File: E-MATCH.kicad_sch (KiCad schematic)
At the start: 23 parts, among them IC1 NCV81071BZR2G, IC2 NCV81071BZR2G, J1 691210910002, J2 691210910002, J3 691210910002, J4 691210910002, J5 DC Jack, Q1 AOSP36326C, Q2 AOSP36326C, Q3 AOSP36326C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

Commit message: Schematic pdf now in the repository
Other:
- title: (none) -> E-match Firing Circuit
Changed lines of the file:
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@@
 	(generator_version "9.0")
 	(paper "A4")
+	(title_block
+		(title "E-match Firing Circuit")
+		(date "2026-01-29")
+		(rev "v1.0")
+	)
 	(rectangle
 		(start 203.708 12.9484)

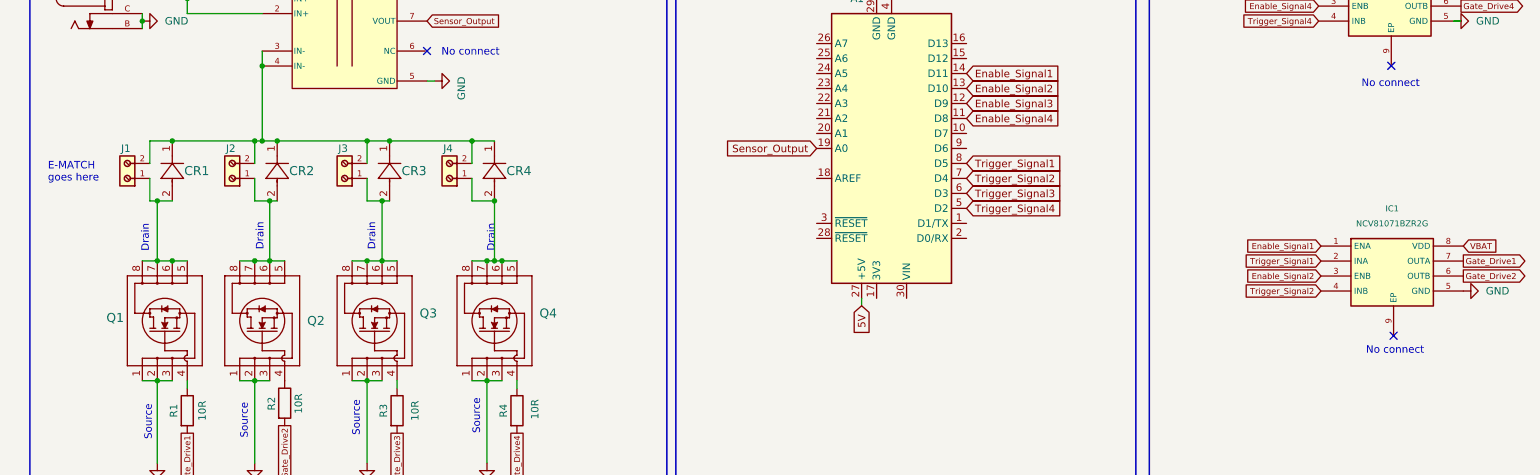
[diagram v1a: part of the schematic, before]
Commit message: modified some footprints
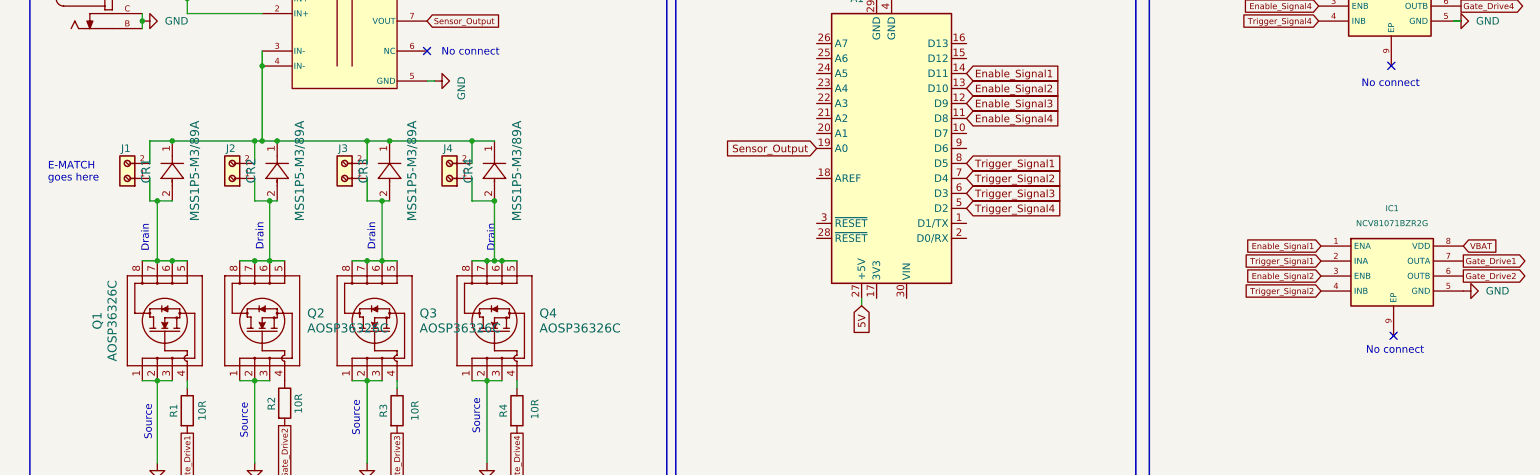
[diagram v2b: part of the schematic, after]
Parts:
- CR1, CR2, CR3, CR4: footprint (none) -> DIODE_MSP3V3
- IC1: footprint (none) -> SOP65P490X110-9N
- Q1, Q2, Q3, Q4: footprint (none) -> SO8SOP-8L_AOS
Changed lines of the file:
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@@
 		(dnp no)
 		(property "Reference" "CR2"
-			(at 57.912 78.74 90)
+			(at 51.435 78.74 0)
 			(effects
 				(font
 					(size 1.524 1.524)
 				)
-				(justify right)
 			)
 		)
 		(property "Value" "MSS1P5-M3/89A"
-			(at 59.69 80.0099 90)
+			(at 59.69 78.74 0)
 			(effects
 				(font
 					(size 1.524 1.524)
 				)
-				(justify right)
-				(hide yes)
-			)
-		)
-		(property "Footprint" ""
+			)
+		)
+		(property "Footprint" "DIODE_MSP3V3"
 			(at 55.88 83.82 0)
 			(effects
@@
 		(dnp no)
 		(property "Reference" "CR3"
-			(at 76.962 78.74 90)
+			(at 70.485 78.74 0)
 			(effects
 				(font
 					(size 1.524 1.524)
 				)
-				(justify right)
 			)
 		)
 		(property "Value" "MSS1P5-M3/89A"
-			(at 78.74 80.0099 90)
+			(at 78.74 78.74 0)
 			(effects
 				(font
 					(size 1.524 1.524)
 				)
-				(justify right)
-				(hide yes)
-			)
-		)
-		(property "Footprint" ""
+			)
+		)
+		(property "Footprint" "DIODE_MSP3V3"
 			(at 74.93 83.82 0)
 			(effects
@@
 		(dnp no)
 		(property "Reference" "CR1"
-			(at 40.132 78.74 90)
+			(at 33.655 78.74 0)
 			(effects
 				(font
 					(size 1.524 1.524)
 				)
-				(justify right)
 			)
 		)
 		(property "Value" "MSS1P5-M3/89A"
-			(at 41.91 80.0099 90)
+			(at 41.91 78.74 0)
 			(effects
 				(font
 					(size 1.524 1.524)
 				)
-				(justify right)
-				(hide yes)
-			)
-		)
-		(property "Footprint" ""
+			)
+		)
+		(property "Footprint" "DIODE_MSP3V3"
 			(at 38.1 83.82 0)
 			(effects
@@
 	)
 	(symbol
-		(lib_name "NCV81071BZR2G_1")
 		(lib_id "Gate Driver:NCV81071BZR2G")
 		(at 232.7997 91.4751 0)
@@
 		(fields_autoplaced yes)
 		(property "Reference" "IC1"
-			(at 244.8647 85.1251 0)
+			(at 244.8647 85.09 0)
 			(effects
 				(font
@@
 		)
 		(property "Value" "NCV81071BZR2G"
-			(at 244.8647 87.6651 0)
+			(at 244.8647 87.63 0)
 			(effects
 				(font
@@
 			)
 		)
-		(property "Footprint" ""
+		(property "Footprint" "SOP65P490X110-9N"
 			(at 259.4697 186.3951 0)
 			(effects
@@
 		(dnp no)
 		(property "Reference" "CR4"
-			(at 94.742 78.74 90)
+			(at 88.265 78.74 0)
 			(effects
 				(font
 					(size 1.524 1.524)
 				)
-				(justify right)
 			)
 		)
 		(property "Value" "MSS1P5-M3/89A"
-			(at 96.52 80.0099 90)
+			(at 96.52 78.74 0)
 			(effects
 				(font
 					(size 1.524 1.524)
 				)
-				(justify right)
-				(hide yes)
-			)
-		)
-		(property "Footprint" ""
+			)
+		)
+		(property "Footprint" "DIODE_MSP3V3"
 			(at 92.71 83.82 0)
 			(effects
@@
 	)
 	(symbol
-		(lib_name "AOSP36326C_1")
 		(lib_id "N-Ch Mosfet:AOSP36326C")
 		(at 88.9 119.38 90)
@@
 				)
 				(justify right)
-				(hide yes)
-			)
-		)
-		(property "Footprint" ""
+			)
+		)
+		(property "Footprint" "SO8SOP-8L_AOS"
 			(at 77.978 104.648 0)
 			(effects
@@
 	)
 	(symbol
-		(lib_name "AOSP36326C_1")
 		(lib_id "N-Ch Mosfet:AOSP36326C")
 		(at 68.58 119.38 90)
@@
 				)
 				(justify right)
-				(hide yes)
-			)
-		)
-		(property "Footprint" ""
+			)
+		)
+		(property "Footprint" "SO8SOP-8L_AOS"
 			(at 57.658 104.648 0)
 			(effects
@@
 		(dnp no)
 		(property "Reference" "Q1"
-			(at 26.924 103.632 90)
+			(at 25.4 104.14 0)
 			(effects
 				(font
 					(size 1.524 1.524)
 				)
-				(justify right)
 			)
 		)
 		(property "Value" "AOSP36326C"
-			(at 43.942 108.712 90)
+			(at 27.94 104.14 0)
 			(effects
 				(font
 					(size 1.524 1.524)
 				)
-				(justify right)
-				(hide yes)
-			)
-		)
-		(property "Footprint" ""
-			(at 28.702 104.14 0)
+			)
+		)
+		(property "Footprint" "SO8SOP-8L_AOS"
+			(at 22.098 104.648 0)
 			(effects
 				(font
@@
 		)
 		(property "Datasheet" "AOSP36326C"
-			(at 28.702 104.14 0)
+			(at 19.558 104.648 0)
 			(effects
 				(font
@@
 	)
 	(symbol
-		(lib_name "AOSP36326C_1")
 		(lib_id "N-Ch Mosfet:AOSP36326C")
 		(at 49.53 119.38 90)
@@
 		(fields_autoplaced yes)
 		(property "Reference" "Q2"
-			(at 60.96 104.1399 90)
+			(at 60.96 102.8699 90)
 			(effects
 				(font
@@
 				)
 				(justify right)
-				(hide yes)
-			)
-		)
-		(property "Footprint" ""
+			)
+		)
+		(property "Footprint" "SO8SOP-8L_AOS"
 			(at 38.608 104.648 0)
 			(effects

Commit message: Cleaned a few footprints
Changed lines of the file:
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@@
-	(wire
-		(pts
-			(xy 81.28 48.26) (xy 81.28 45.72)
-		)
-		(stroke
-			(width 0)
-			(type default)
-		)
-	)
 	(wire
 		(pts

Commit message: added a decoupling capacitor
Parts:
- added C1: 0.1u, 0.1 uF Cap:CAP_C0603C104K5RAC3121_KEM-L, symbol Device:C
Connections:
- net 5V: now also C1.2
- net GND: now also C1.1
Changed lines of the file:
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@@
+	)
+	(junction
+		(at 81.28 48.26)
+		(diameter 0)
+		(color 0 0 0 0)
 	)
 	(junction
@@
 	(wire
 		(pts
+			(xy 85.09 48.26) (xy 81.28 48.26)
+		)
+		(stroke
+			(width 0)
+			(type default)
+		)
+	)
+	(wire
+		(pts
 			(xy 71.12 114.3) (xy 71.12 128.27)
 		)
@@
 		(pts
 			(xy 88.9 83.82) (xy 92.71 83.82)
+		)
+		(stroke
+			(width 0)
+			(type default)
+		)
+	)
+	(wire
+		(pts
+			(xy 81.28 46.99) (xy 81.28 48.26)
 		)
 		(stroke
@@
 	(global_label "5V"
 		(shape input)
-		(at 81.28 48.26 0)
+		(at 85.09 48.26 0)
 		(fields_autoplaced yes)
 		(effects
@@
 		)
 		(property "Intersheetrefs" "${INTERSHEET_REFS}"
-			(at 85.5064 48.26 0)
+			(at 89.3164 48.26 0)
 			(effects
 				(font
@@
 				(path "/ac49d8b8-9946-4b6b-9646-a2b20606c52a"
 					(reference "#PWR08")
+					(unit 1)
+				)
+			)
+		)
+	)
+	(symbol
+		(lib_id "power:GND")
+		(at 81.28 39.37 180)
+		(unit 1)
+		(exclude_from_sim no)
+		(in_bom yes)
+		(on_board yes)
+		(dnp no)
+		(property "Reference" "#PWR011"
+			(at 81.28 33.02 0)
+			(effects
+				(font
+					(size 1.27 1.27)
+				)
+				(hide yes)
+			)
+		)
+		(property "Value" "GND"
+			(at 80.518 34.798 0)
+			(effects
+				(font
+					(size 1.27 1.27)
+				)
+				(justify right)
+			)
+		)
+		(property "Footprint" ""
+			(at 81.28 39.37 0)
+			(effects
+				(font
+					(size 1.27 1.27)
+				)
+				(hide yes)
+			)
+		)
+		(property "Datasheet" ""
+			(at 81.28 39.37 0)
+			(effects
+				(font
+					(size 1.27 1.27)
+				)
+				(hide yes)
+			)
+		)
+		(property "Description" "Power symbol creates a global label with name \"GND\" , ground"
+			(at 81.28 39.37 0)
+			(effects
+				(font
+					(size 1.27 1.27)
+				)
+				(hide yes)
+			)
+		)
+		(pin "1"
+		)
+		(instances
+			(project "E-MATCH"
+				(path "/ac49d8b8-9946-4b6b-9646-a2b20606c52a"
+					(reference "#PWR011")
 					(unit 1)
 				)
@@
 					(unit 1)
 				)
+			)
+		)
+	)
+	(symbol
+		(lib_id "Device:C")
+		(at 81.28 43.18 0)
+		(unit 1)
+		(exclude_from_sim no)
+		(in_bom yes)
+		(on_board yes)
+		(dnp no)
+		(fields_autoplaced yes)
+		(property "Reference" "C1"
+			(at 85.09 41.9099 0)
+			(effects
+				(font
+					(size 1.27 1.27)
+				)
+				(justify left)
+			)
+		)
+		(property "Value" "0.1u"
+			(at 85.09 44.4499 0)
+			(effects
+				(font
+					(size 1.27 1.27)
+				)
+				(justify left)
+			)
+		)
+		(property "Footprint" "0.1 uF Cap:CAP_C0603C104K5RAC3121_KEM-L"
+			(at 82.2452 46.99 0)
+			(effects
+				(font
+					(size 1.27 1.27)
+				)
+				(hide yes)
+			)
+		)
+		(property "Datasheet" "~"
+			(at 81.28 43.18 0)
+			(effects
+				(font
+					(size 1.27 1.27)
+				)
+				(hide yes)
+			)
+		)
+		(property "Description" "Unpolarized capacitor"
+			(at 81.28 43.18 0)
+			(effects
+				(font
+					(size 1.27 1.27)
+				)
+				(hide yes)
+			)
+		)
+		(pin "2"
+		)
+		(pin "1"
+		)
+		(instances
+			(project ""
+				(path "/ac49d8b8-9946-4b6b-9646-a2b20606c52a"
+					(reference "C1")
+					(unit 1)
+				)

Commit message: made minor adjustments in both schematic and pcb layout
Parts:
- removed C1: 0.1u, 0.1 uF Cap:CAP_C0603C104K5RAC3121_KEM-L, symbol Device:C
- added C4, C5, C6: C_Small, Capacitor_SMD:C_0603_1608Metric, symbol Device:C_Small
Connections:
- net 5V: now also C4.2
- net GND: now also C4.1, C5.1, C6.1
- net VBAT: now also C5.2, C6.2

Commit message: some changes
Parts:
- added M1: FDC8878, SuperSot6_SOT-23-6_1P6X2P9_ONS, symbol FDC8878:FDC8878
- added Q5: FDD1600N10ALZ, FDD1600N10ALZ:TO252_FDD1600_ONS-L, symbol FDD1600N10ALZ:FDD1600N10ALZ
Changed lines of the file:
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@@
+	)
+	(symbol
+		(lib_id "FDC8878:FDC8878")
+		(at 134.62 125.73 0)
+		(unit 1)
+		(exclude_from_sim no)
+		(in_bom yes)
+		(on_board yes)
+		(dnp no)
+		(fields_autoplaced yes)
+		(property "Reference" "M1"
+			(at 154.94 115.57 0)
+			(effects
+				(font
+					(size 1.524 1.524)
+				)
+			)
+		)
+		(property "Value" "FDC8878"
+			(at 154.94 118.11 0)
+			(effects
+				(font
+					(size 1.524 1.524)
+				)
+			)
+		)
+		(property "Footprint" "SuperSot6_SOT-23-6_1P6X2P9_ONS"
+			(at 134.62 125.73 0)
+			(effects
+				(font
+					(size 1.27 1.27)
+					(italic yes)
+				)
+				(hide yes)
+			)
+		)
+		(property "Datasheet" "FDC8878"
+			(at 134.62 125.73 0)
+			(effects
+				(font
+					(size 1.27 1.27)
+					(italic yes)
+				)
+				(hide yes)
+			)
+		)
+		(property "Description" ""
+			(at 134.62 125.73 0)
+			(effects
+				(font
+					(size 1.27 1.27)
+				)
+				(hide yes)
+			)
+		)
+		(pin "5"
+		)
+		(pin "6"
+		)
+		(pin "3"
+		)
+		(pin "2"
+		)
+		(pin "1"
+		)
+		(pin "4"
+		)
+		(instances
+			(project ""
+				(path "/ac49d8b8-9946-4b6b-9646-a2b20606c52a"
+					(reference "M1")
+					(unit 1)
+				)
+			)
+		)
 	)
 	(symbol
@@
 					(unit 1)
 				)
+			)
+		)
+	)
+	(symbol
+		(lib_id "FDD1600N10ALZ:FDD1600N10ALZ")
+		(at 234.95 132.08 0)
+		(unit 1)
+		(exclude_from_sim no)
+		(in_bom yes)
+		(on_board yes)
+		(dnp no)
+		(fields_autoplaced yes)
+		(property "Reference" "Q5"
+			(at 251.46 130.8099 0)
+			(effects
+				(font
+					(size 1.524 1.524)
+				)
+				(justify left)
+			)
+		)
+		(property "Value" "FDD1600N10ALZ"
+			(at 251.46 133.3499 0)
+			(effects
+				(font
+					(size 1.524 1.524)
+				)
+				(justify left)
+			)
+		)
+		(property "Footprint" "FDD1600N10ALZ:TO252_FDD1600_ONS-L"
+			(at 234.95 132.08 0)
+			(effects
+				(font
+					(size 1.27 1.27)
+					(italic yes)
+				)
+				(hide yes)
+			)
+		)
+		(property "Datasheet" "FDD1600N10ALZ"
+			(at 234.95 132.08 0)
+			(effects
+				(font
+					(size 1.27 1.27)
+					(italic yes)
+				)
+				(hide yes)
+			)
+		)
+		(property "Description" ""
+			(at 234.95 132.08 0)
+			(effects
+				(font
+					(size 1.27 1.27)
+				)
+				(hide yes)
+			)
+		)
+		(pin "1"
+		)
+		(pin "3"
+		)
+		(pin "2"
+		)
+		(instances
+			(project ""
+				(path "/ac49d8b8-9946-4b6b-9646-a2b20606c52a"
+					(reference "Q5")
+					(unit 1)
+				)
